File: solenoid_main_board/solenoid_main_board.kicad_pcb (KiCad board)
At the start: 2 copper layers, 21.8 x 35.5 mm, 12 parts, among them J3 1x2 5.08, U1 solenoid_module, U2 Control_panel_module_comm, U3 LM78M05, U4 MCU_module

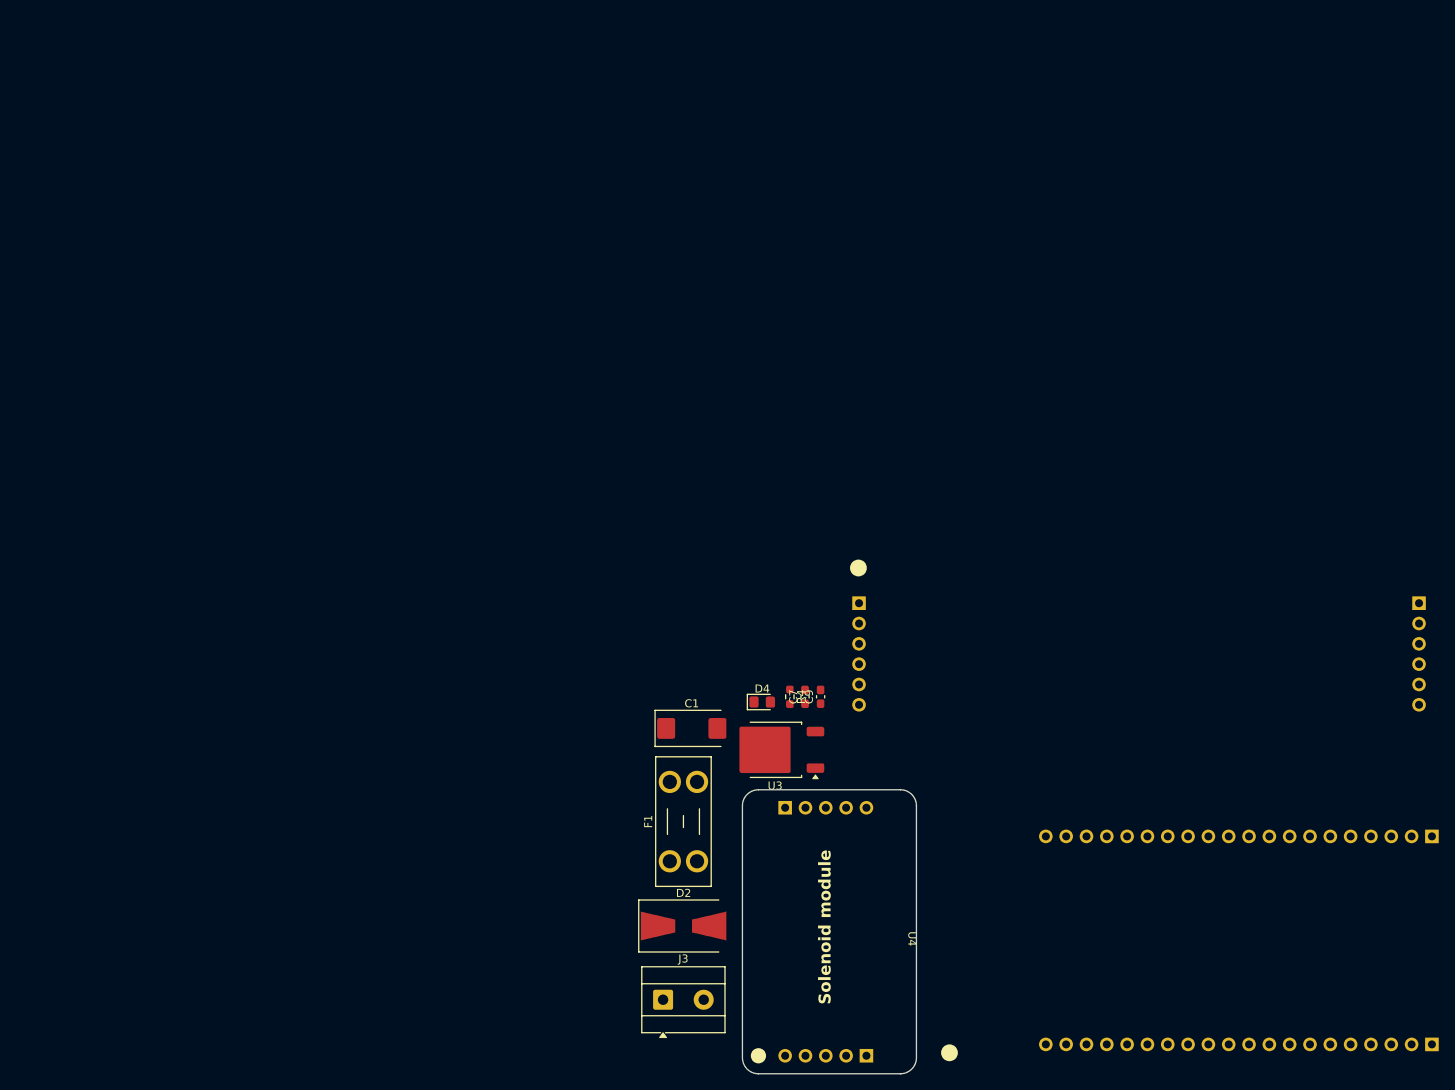
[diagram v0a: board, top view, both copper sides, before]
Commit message: Solenoid main board finished
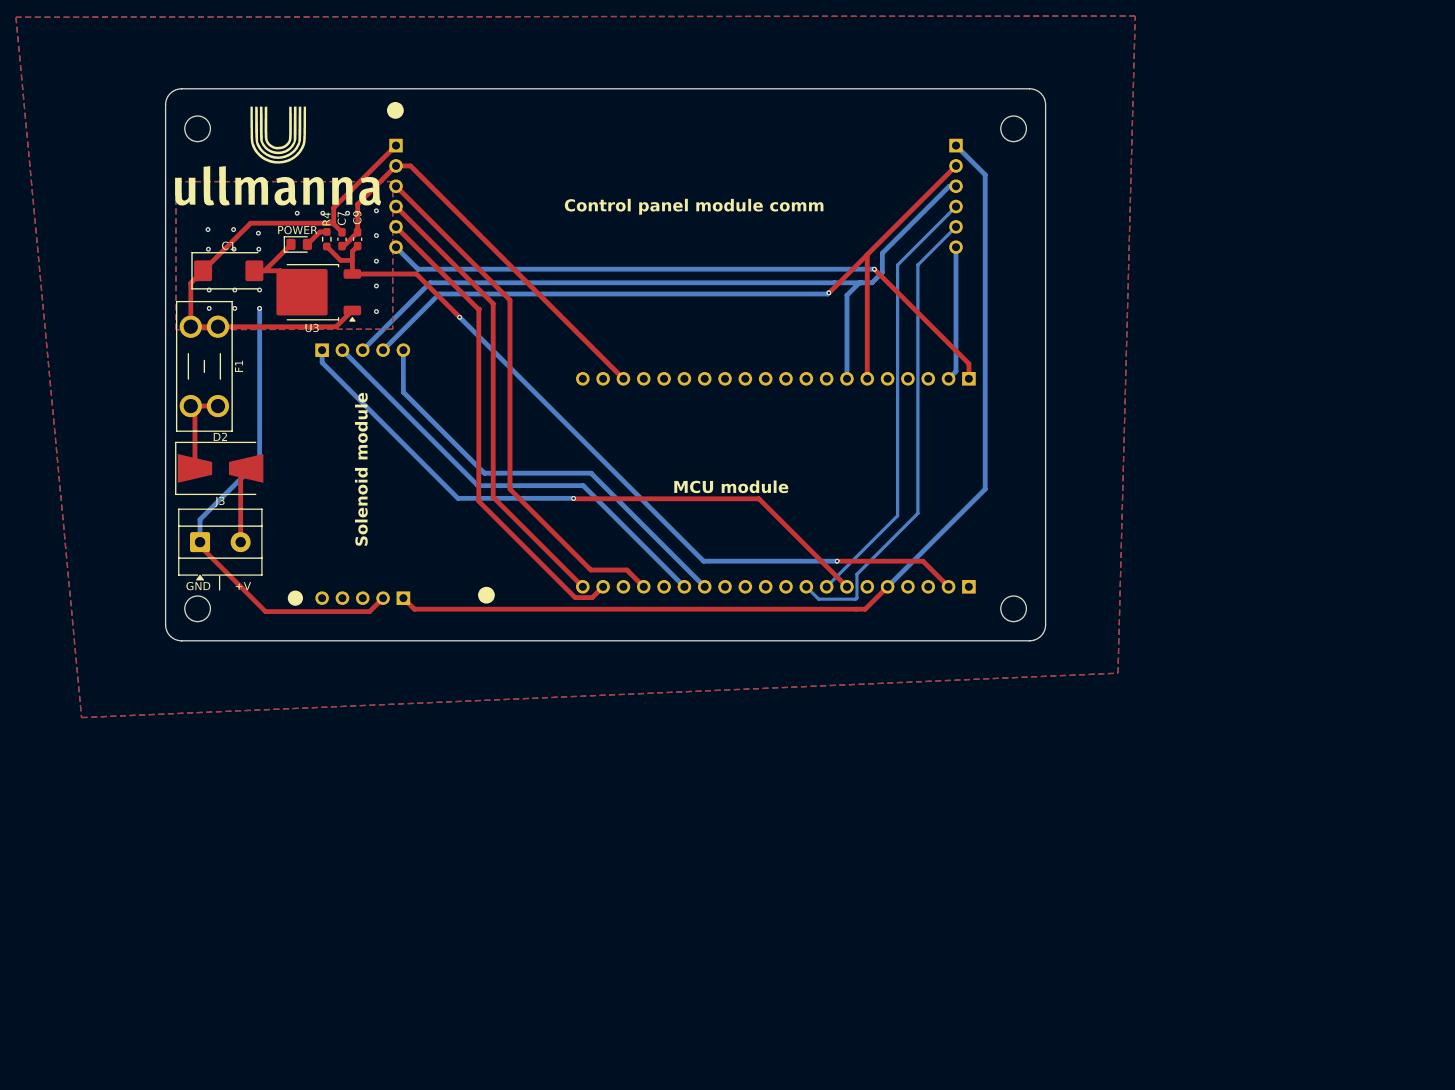
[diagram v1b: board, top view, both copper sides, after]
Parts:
- added G***: LOGO, LOGO, F.Cu at (56.7, 41.1)
- added H3: MountingHole, MountingHole:MountingHole_3.2mm_M3, F.Cu at (148.6, 36.3)
- added H3: MountingHole, MountingHole:MountingHole_3.2mm_M3, F.Cu at (148.6, 96.3)
- added H3: MountingHole, MountingHole:MountingHole_3.2mm_M3, F.Cu at (46.6, 96.3)
- added H3: MountingHole, MountingHole:MountingHole_3.2mm_M3, F.Cu at (46.6, 36.3)
- moved F1 87.5 mm to (49.2, 61.0), turned to -90 degrees
- moved U3 81.4 mm to (60.9, 56.7)
- moved C1 81.4 mm to (50.5, 54.0)
- moved C7 81.4 mm to (64.7, 50.1), turned to -90 degrees
- moved C9 81.4 mm to (66.6, 50.1)
- moved U2 81.4 mm to (107.6, 45.3)
- moved U4 81.4 mm to (113.7, 80.5)
- moved D2 81.4 mm to (49.5, 78.8)
- moved D4 81.4 mm to (59.3, 50.8)
- moved J3 81.4 mm to (46.9, 88.0)
- moved R4 81.4 mm to (62.8, 50.1)
- moved U1 81.4 mm to (66.9, 79.4)
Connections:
- C1 pad 1: Net-(U3-VI) -> +VDD
- C7 pad 1: Net-(U3-VI) -> +VDD
- D2 pad 2: +VDD -> /power_supply/+V_IN
- F1 pad 1: Net-(U3-VI) -> +VDD
- J3 pad 2: +VDD -> /power_supply/+V_IN
- U3 pad 1: Net-(U3-VI) -> +VDD
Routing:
- net GND: track 0.00 -> 124.7 mm, vias 0 -> 20
- net +3.3V: track 0.00 -> 124.0 mm
- net +5V: track 0.00 -> 98.4 mm, vias 0 -> 2
- net SCL: track 0.00 -> 97.0 mm
- net SDA: track 0.00 -> 96.7 mm, vias 0 -> 1
- net TX: track 0.00 -> 79.5 mm, vias 0 -> 1
- net Net-(U1-IHall): track 0.00 -> 78.8 mm, vias 0 -> 1
- net Net-(U2-SW_MODE): track 0.00 -> 65.5 mm
- net +VDD: track 0.00 -> 62.0 mm
- net Net-(U2-LED_STATUS): track 0.00 -> 59.8 mm
- net Net-(U2-RV1): track 0.00 -> 58.5 mm
- net Net-(U2-LED_ERR): track 0.00 -> 57.2 mm
- net Net-(U1-A/R): track 0.00 -> 55.0 mm
- net AGND: track 0.00 -> 54.2 mm
- net Net-(U1-FB): track 0.00 -> 53.0 mm
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- added copper zone on B.Cu, net (none)
- added copper zone on F.Cu, net (none)
- added copper zone on B.Cu, net GND
- added copper zone on F.Cu, net GND
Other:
- board size 21.8 x 35.5 mm -> 110 x 69 mm
- board text added: "+V"
- board text added: "Control panel module comm"
- board text added: "GND"
- board text added: "MCU module"
- board text added: "POWER"

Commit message: PCB update
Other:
- board text added: "Solenoid_testbench_module v1.0.0"
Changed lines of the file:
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@@
+		)
+	)
+	(gr_text "Solenoid_testbench_module\nv1.0.0"
+		(at 150.05 88.75 0)
+		(layer "B.SilkS")
+		(effects
+			(font
+				(size 1.5 1.5)
+				(thickness 0.2)
+				(bold yes)
+			)
+			(justify left bottom mirror)
 		)
 	)
